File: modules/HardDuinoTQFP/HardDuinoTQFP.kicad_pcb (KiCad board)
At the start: 2 copper layers, 40.6 x 40.6 mm, 27 parts, among them J1 Conn_01x10_Male, J2 Conn_01x10_Male, J3 Conn_01x05_Male, J4 Conn_02x03_Odd_Even, J5 Conn_01x01_Male, Q1 IRLML5203, U1 ATmega328P-AU, Y1 16MHz

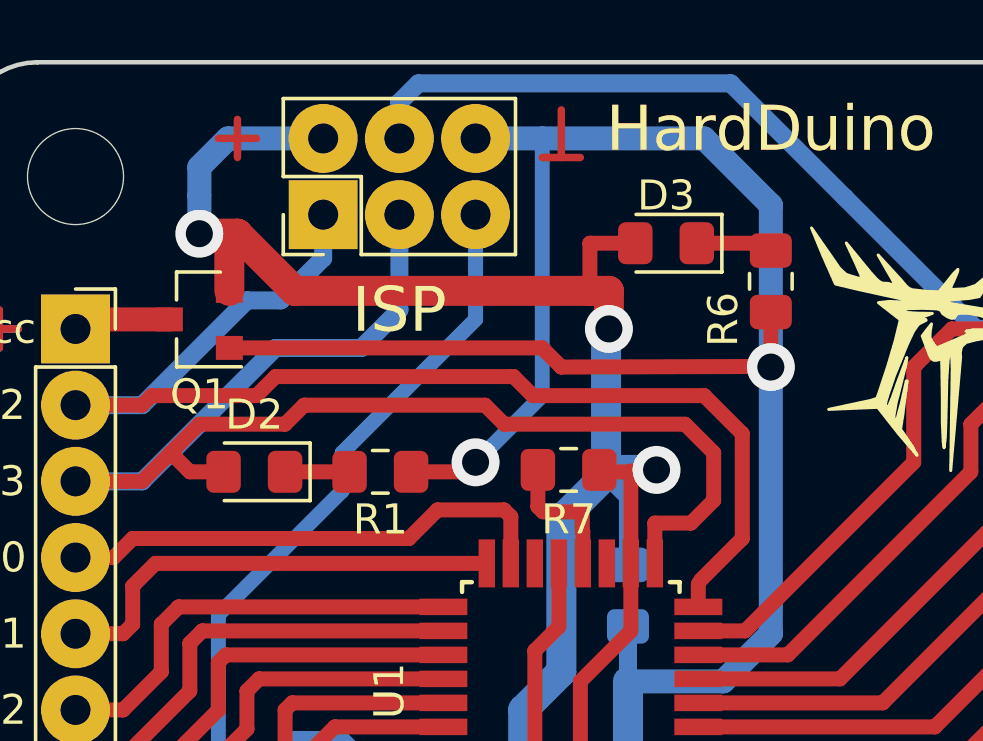
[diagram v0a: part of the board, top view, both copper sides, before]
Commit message: Add labels
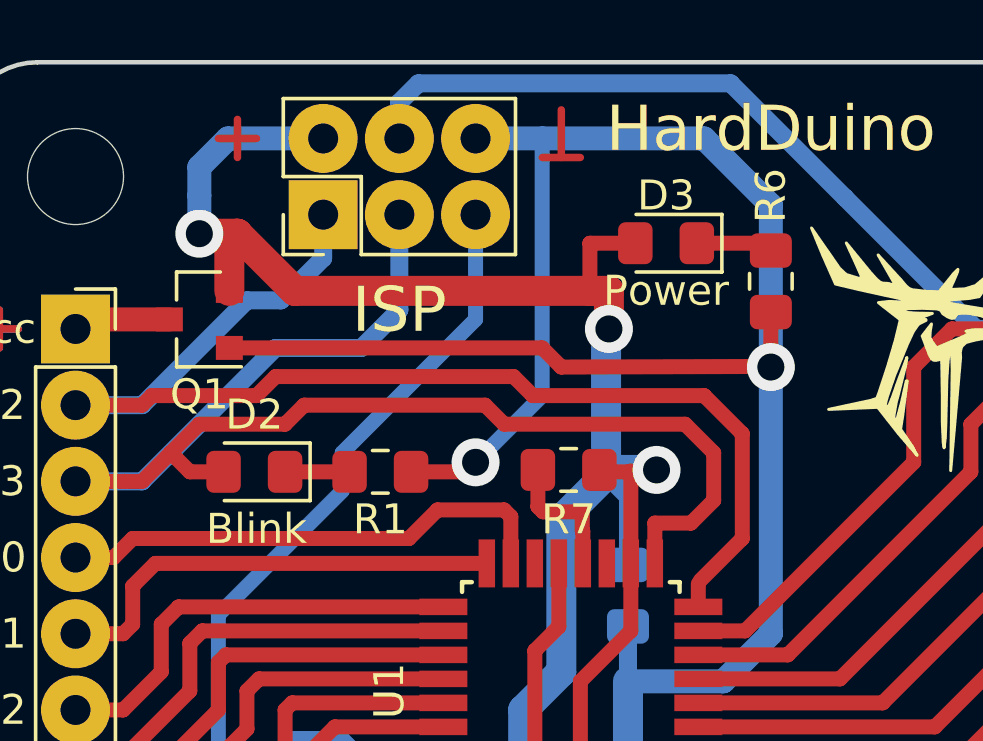
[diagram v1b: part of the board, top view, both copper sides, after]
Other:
- board text added: "Blink"
- board text added: "Power"

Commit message: Fix hash, add gerber
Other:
- rule solder_mask_min_width: 0.25 -> 0.1
- board text added: "11.11.2020"
- board text added: "f58a85"
- board text removed: "05.06.2020"
- board text removed: "2effdf"

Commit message: HardDuino small fixes
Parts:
- moved R1 16.5 mm to (90.2, 62.2), turned to 270 degrees
- moved D2 8.89 mm to (90.2, 54.4), turned to 90 degrees
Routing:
- net GND: track 134.4 -> 129.0 mm, vias 3 -> 2
- net Net-(D2-Pad1): track 2.15 -> 5.81 mm
- net /13: track 46.5 -> 48.2 mm

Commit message: HardDuinoTQFP. Fix hash, add gerber...
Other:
- board text added: "23.11.2020"
- board text added: "9f7f9f"
- board text removed: "11.11.2020"
- board text removed: "f58a85"

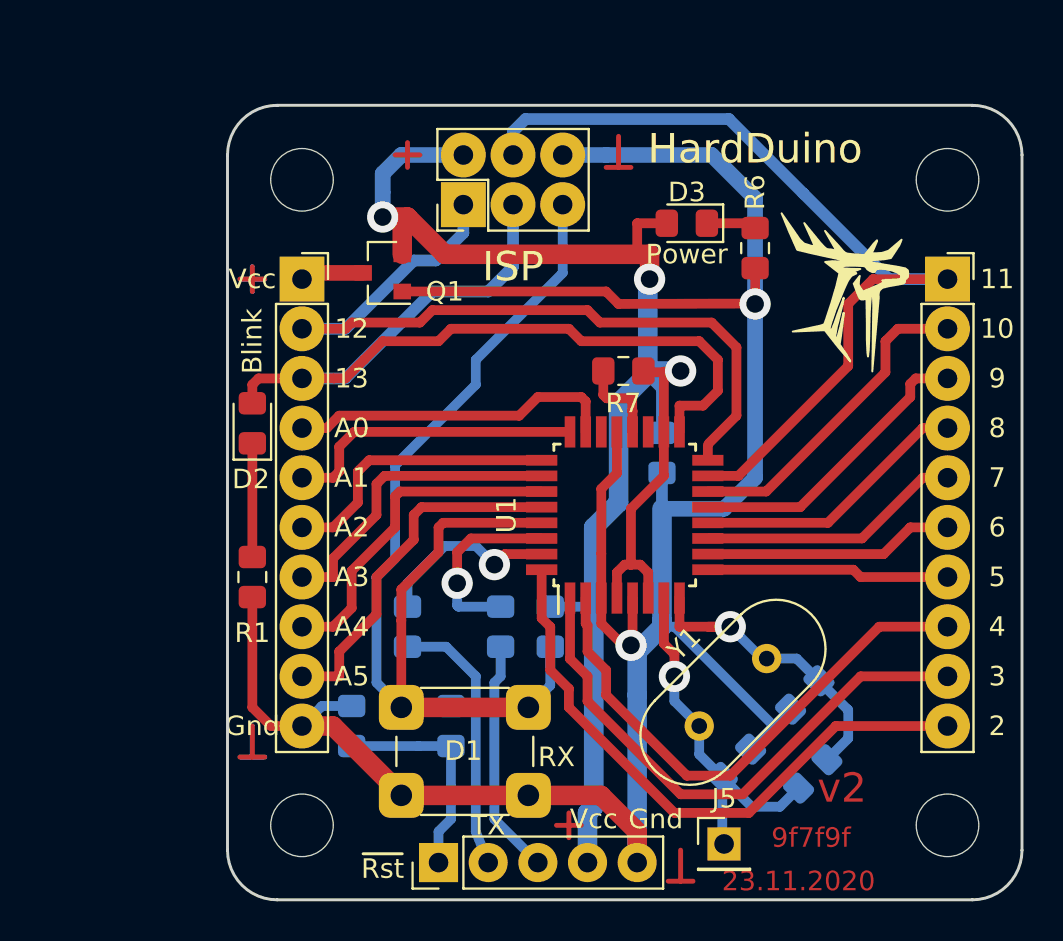
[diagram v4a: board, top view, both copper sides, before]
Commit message: 1x PCBs. Move holes to edges. Caution! This changes is uncompatible with previous versions...
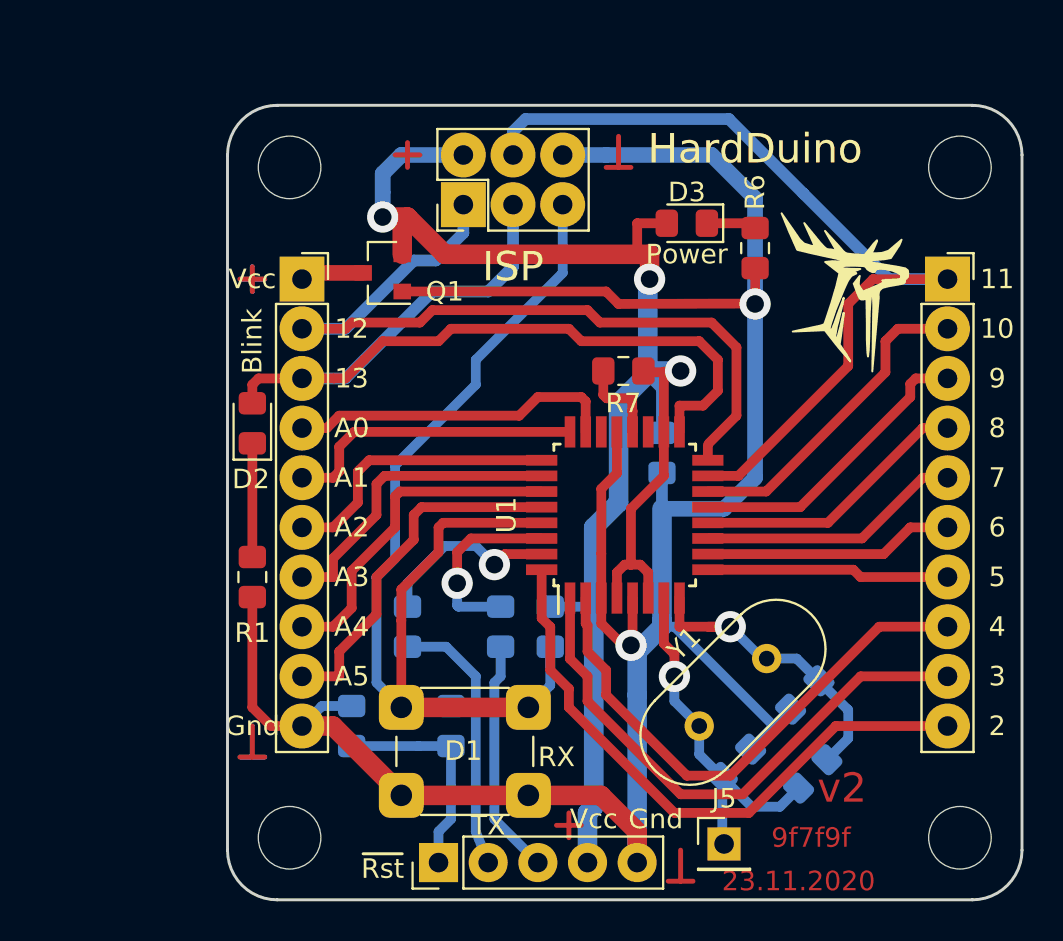
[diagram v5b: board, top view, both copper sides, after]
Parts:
- moved H1 0.90 mm to (92.1, 41.3)
- moved H3 0.90 mm to (126.4, 41.3)
- moved H2 0.90 mm to (92.1, 75.6)
- moved H4 0.90 mm to (126.4, 75.6)
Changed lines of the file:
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@@
   )
   (module MountingHole:MountingHole_3.2mm_M3 (layer F.Cu)
-    (at 92.71 41.91)
+    (at 92.0750 41.2750)
     (descr "Mounting Hole 3.2mm, no annular, M3")
     (tags "mounting hole 3.2mm no annular m3")
@@
   )
   (module MountingHole:MountingHole_3.2mm_M3 (layer F.Cu)
-    (at 92.71 74.93)
+    (at 92.0750 75.5650)
     (descr "Mounting Hole 3.2mm, no annular, M3")
     (tags "mounting hole 3.2mm no annular m3")
@@
   )
   (module MountingHole:MountingHole_3.2mm_M3 (layer F.Cu)
-    (at 125.73 41.91)
+    (at 126.3650 41.2750)
     (descr "Mounting Hole 3.2mm, no annular, M3")
     (tags "mounting hole 3.2mm no annular m3")
@@
   )
   (module MountingHole:MountingHole_3.2mm_M3 (layer F.Cu)
-    (at 125.73 74.93)
+    (at 126.3650 75.5650)
     (descr "Mounting Hole 3.2mm, no annular, M3")
     (tags "mounting hole 3.2mm no annular m3")

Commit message: Fix hash & version
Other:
- board text added: "21.02.2021"
- board text added: "b4d799"
- board text added: "v2.3"
- board text removed: "23.11.2020"
- board text removed: "9f7f9f"
- board text removed: "v2"

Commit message: Fix hashes
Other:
- board text added: "23.02.2021"
- board text added: "513641"
- board text removed: "21.02.2021"
- board text removed: "b4d799"

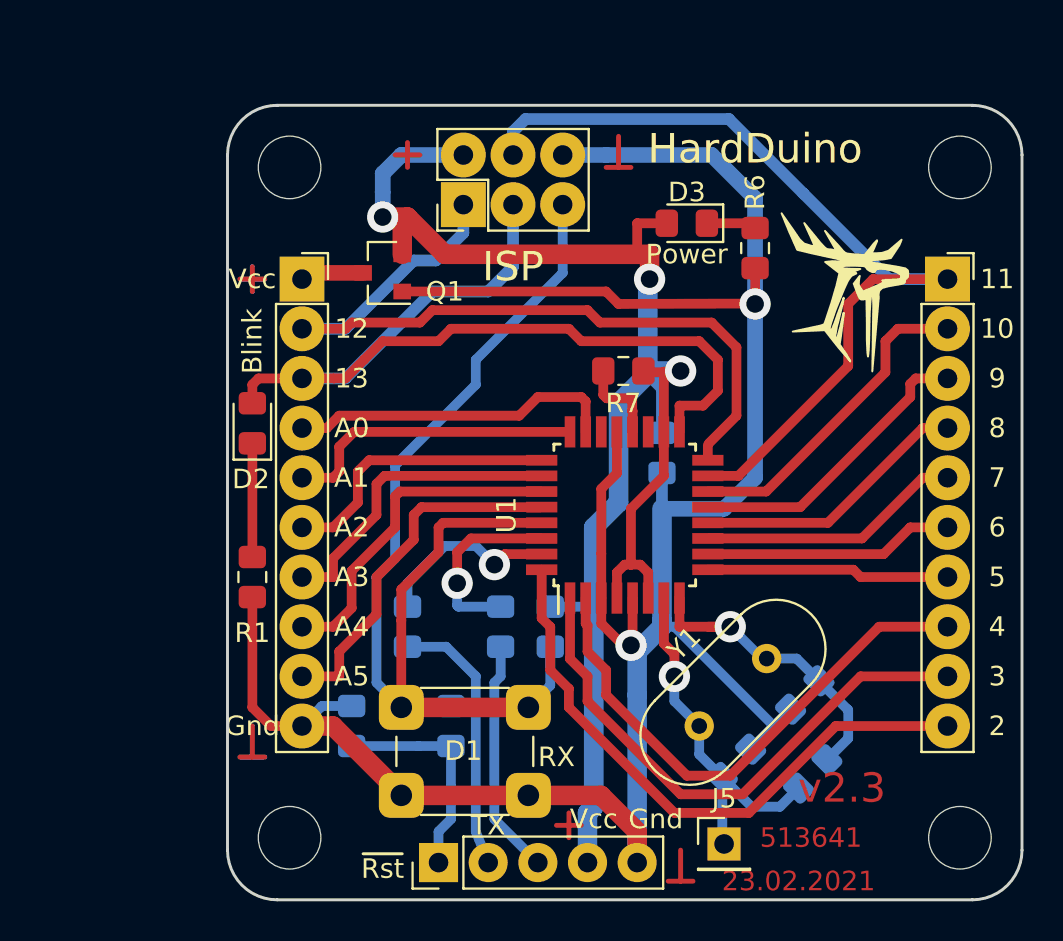
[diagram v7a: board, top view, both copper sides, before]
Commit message: All 1x shields was rotated clockwise
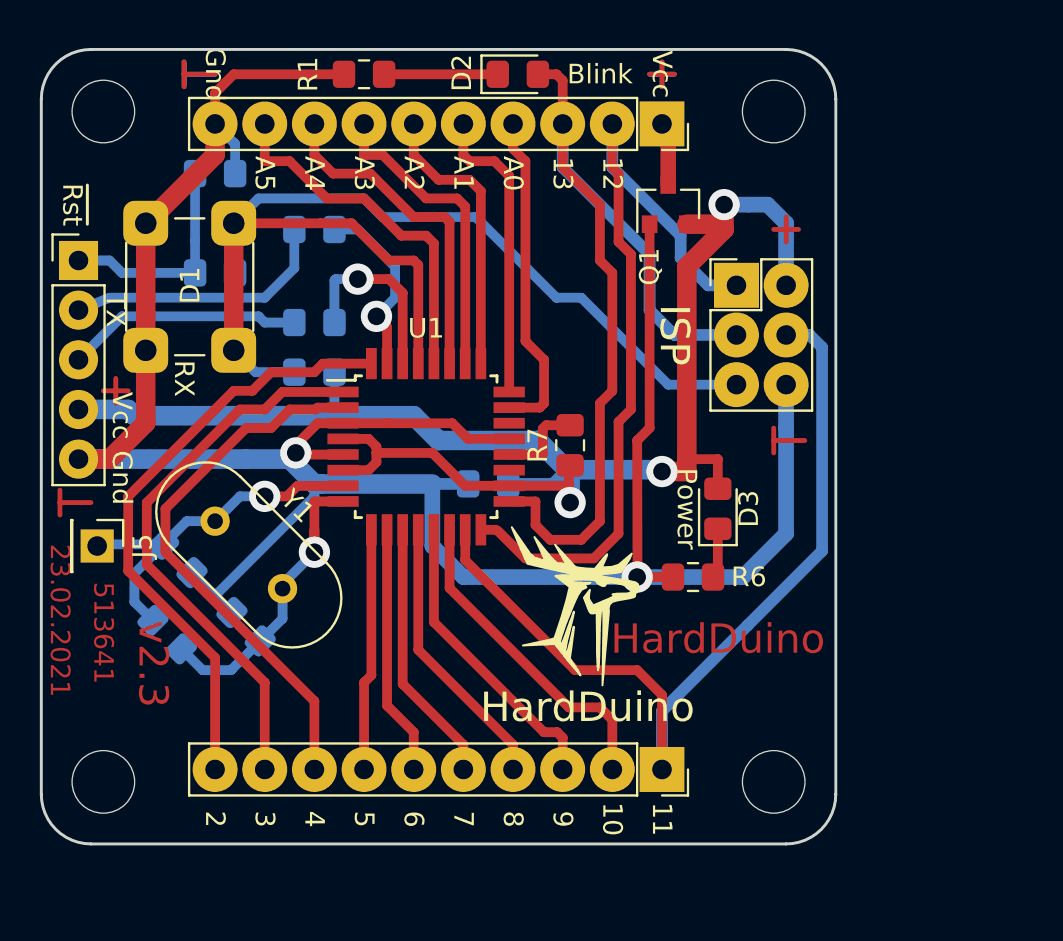
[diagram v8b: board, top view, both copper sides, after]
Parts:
- moved H4 43.9 mm to (82.5, 72.7), turned to 270 degrees
- moved H2 38.3 mm to (82.5, 38.4), turned to 270 degrees
- moved J3 35.9 mm to (81.3, 46.0), turned to 0 degrees
- moved J5 35.5 mm to (82.2, 60.6), turned to 270 degrees
- moved R8 33.8 mm to (85.8, 65.2), turned to 315 degrees
- moved H3 32.8 mm to (116.8, 72.7), turned to 270 degrees
- moved C2 30.4 mm to (86.4, 61.3), turned to 315 degrees
- moved R2 29.1 mm to (88.3, 41.6), turned to 180 degrees
- moved J2 29.0 mm to (111.1, 72.1), turned to 270 degrees
- moved C3 28.8 mm to (89.9, 64.8), turned to 315 degrees
- moved Y1 26.9 mm to (88.3, 59.4), turned to 315 degrees
- moved R1 26.3 mm to (95.9, 36.5), turned to 180 degrees
- moved D1 26.2 mm to (89.2, 44.1), turned to 270 degrees
- moved C1 26.1 mm to (88.3, 46.7), turned to 180 degrees
- moved H1 24.9 mm to (116.8, 38.4), turned to 270 degrees
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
